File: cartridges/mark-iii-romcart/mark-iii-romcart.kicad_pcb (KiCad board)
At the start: 2 copper layers, 72 x 70.5 mm, 6 parts, among them SW1 SW_SPDT, U1 27C512, U2 SG-1000-Cart

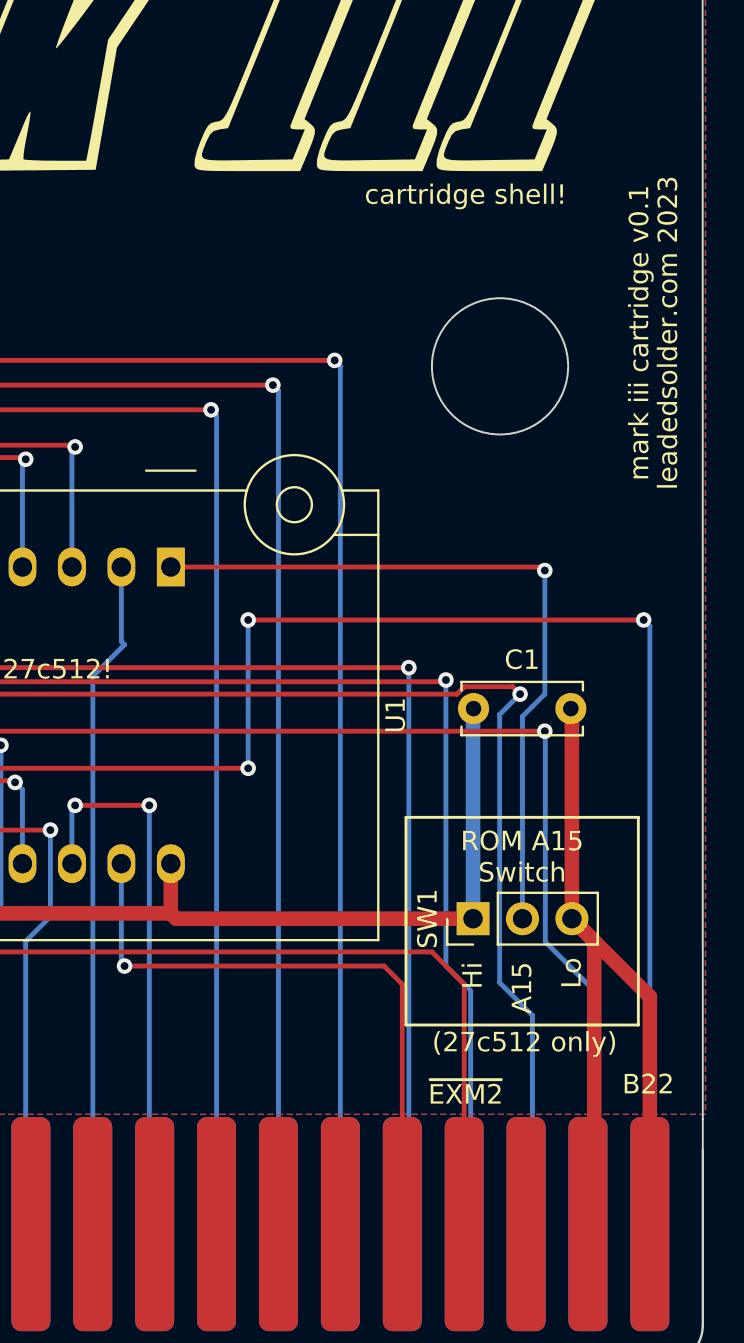
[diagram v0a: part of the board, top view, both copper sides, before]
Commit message: V2 of Mark III cart: 27c64 support without bodge
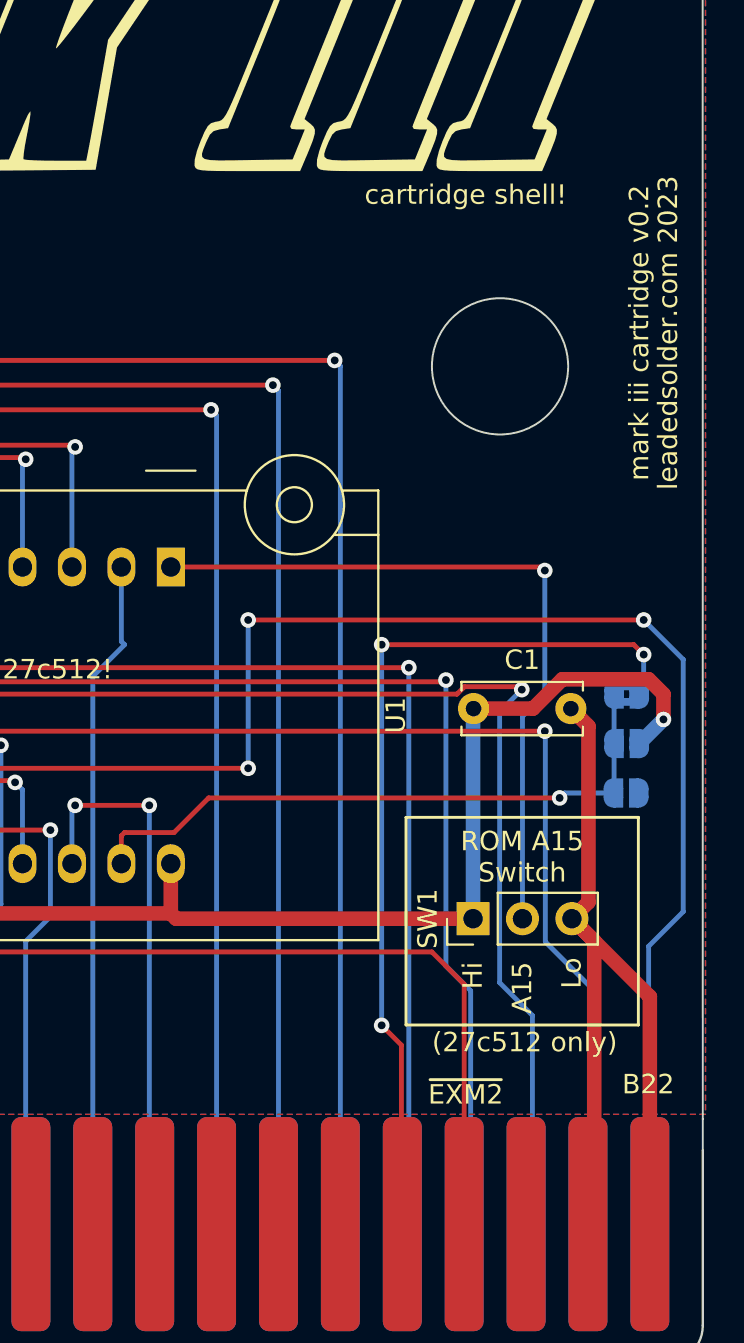
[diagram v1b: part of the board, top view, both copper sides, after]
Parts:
- added JP2: Jumper_2_Bridged, Jumper:SolderJumper-2_P1.3mm_Bridged2Bar_RoundedPad1.0x1.5mm, B.Cu at (93.1, 53.3)
- added JP3: Jumper_2_Open, Jumper:SolderJumper-2_P1.3mm_Open_RoundedPad1.0x1.5mm, B.Cu at (93.1, 58.4)
- added JP4: Jumper_2_Open, Jumper:SolderJumper-2_P1.3mm_Open_RoundedPad1.0x1.5mm, B.Cu at (93.1, 55.9)
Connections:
- U2 pad B18: /A14 -> /CPU_A14
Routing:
- net /CPU_A14: track 0.00 -> 46.0 mm, vias 0 -> 3
- net /5V: track 85.7 -> 99.4 mm, vias 0 -> 1
- net /D7: track 92.4 -> 93.9 mm
- net /GND: track 44.5 -> 45.2 mm
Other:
- board text added: "5V"
- board text added: "A14 select 27c64: use 5V"
- board text added: "GND"
- board text added: "a14"
- board text added: "mark iii cartridge v0.2"
- board text removed: "mark iii cartridge v0.1"

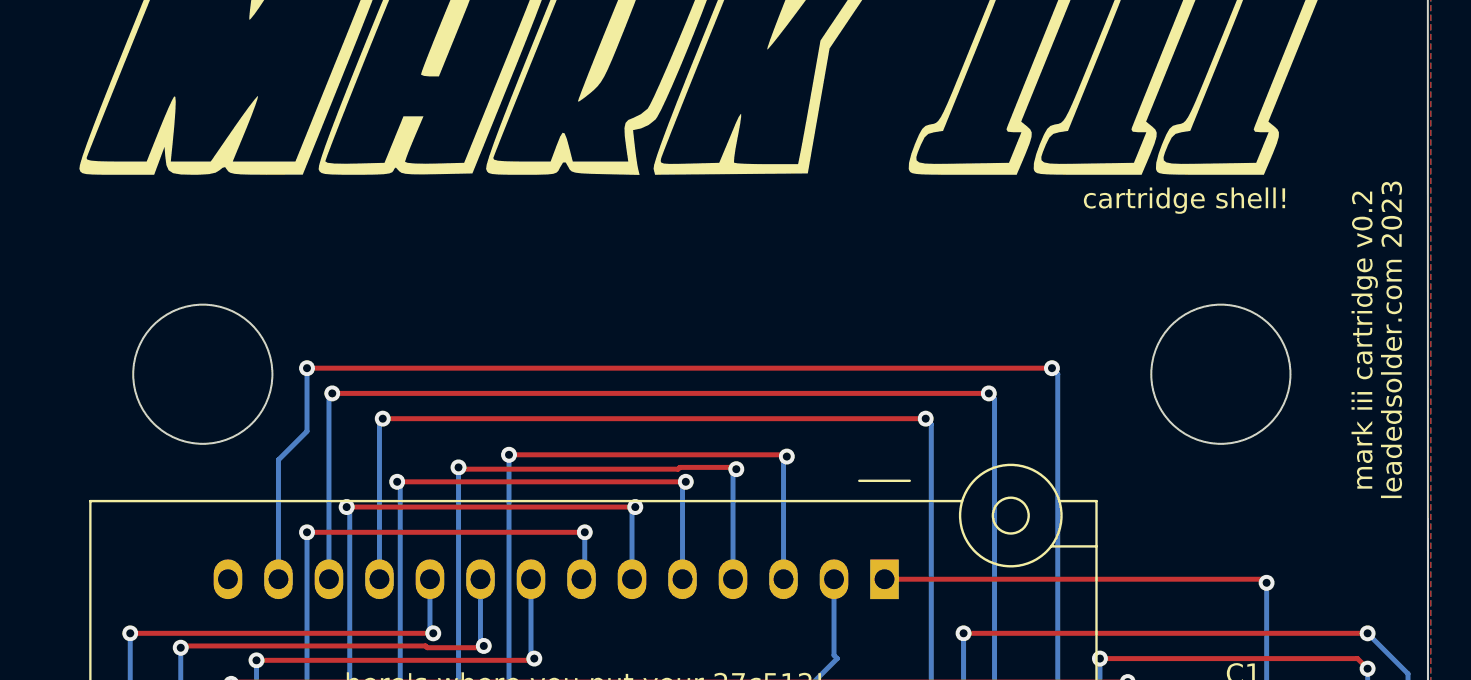
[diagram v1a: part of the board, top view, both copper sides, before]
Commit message: Mark III cart: make holes bigger, move outward 1/2-mm
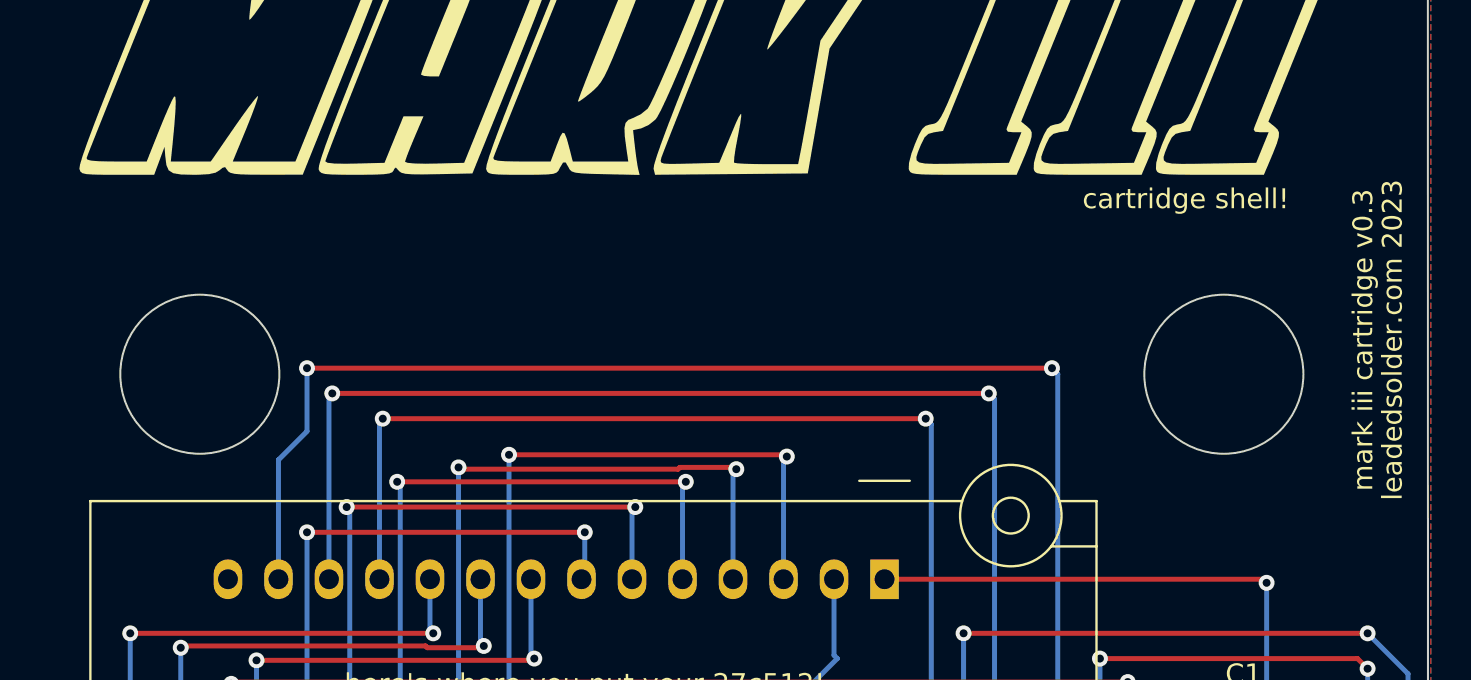
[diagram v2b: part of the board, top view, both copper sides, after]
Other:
- outline, holes or cut-outs redrawn
- board text added: "mark iii cartridge v0.3"
- board text removed: "mark iii cartridge v0.2"
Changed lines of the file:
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@@
   (gr_rect (start 97.263 88.373) (end 24.492 75.292) (layer "B.Mask") (width 0.15) (fill solid))
   (gr_rect (start 97.263 75.292) (end 24.492 88.881) (layer "F.Mask") (width 0.15) (fill solid))
-  (gr_circle (center 35.4 36.5) (end 38.9 36.5) (layer "Edge.Cuts") (width 0.1) (fill none))
-  (gr_circle (center 86.6 36.5) (end 90.1 36.5) (layer "Edge.Cuts") (width 0.1) (fill none))
+  (gr_circle (center 35.25 36.5) (end 39.25 36.5) (layer "Edge.Cuts") (width 0.1) (fill none))
+  (gr_circle (center 86.75 36.5) (end 90.75 36.5) (layer "Edge.Cuts") (width 0.1) (fill none))
   (gr_line (start 97.017 75.169) (end 97.017 76.769) (layer "Edge.Cuts") (width 0.1))
   (gr_line (start 25.017 75.169) (end 25.017 76.769) (layer "Edge.Cuts") (width 0.1))
@@
     (effects (font (size 1 1) (thickness 0.15)))
   )
-  (gr_text "mark iii cartridge v0.2" (at 93.75 34.779001 90) (layer "F.SilkS")
+  (gr_text "mark iii cartridge v0.3" (at 93.75 34.779001 90) (layer "F.SilkS")
     (effects (font (size 1 1) (thickness 0.15)))
   )
